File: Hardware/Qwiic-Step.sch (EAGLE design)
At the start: 53 parts, among them J1 PTH, J2 Qwiic Right Angle, J3 POWER_JACKSUPER_BOMB_DIGITY, J4 Qwiic Right Angle, J5 ISP, U1 A49885MM, U2 ATMEGA328P_TQFP, Y1 16MHz

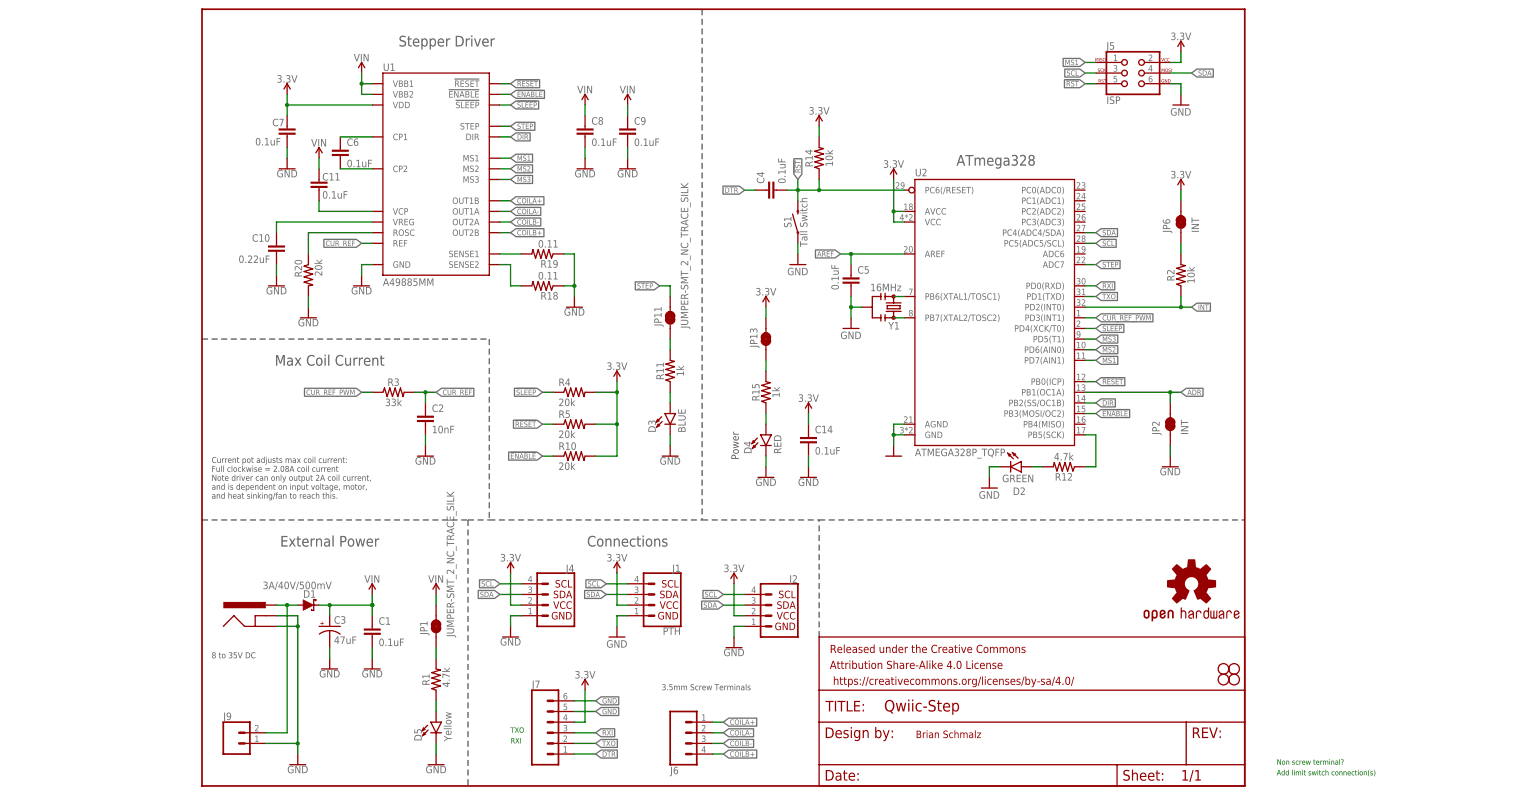
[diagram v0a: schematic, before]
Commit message: New board layout. Added current sense.
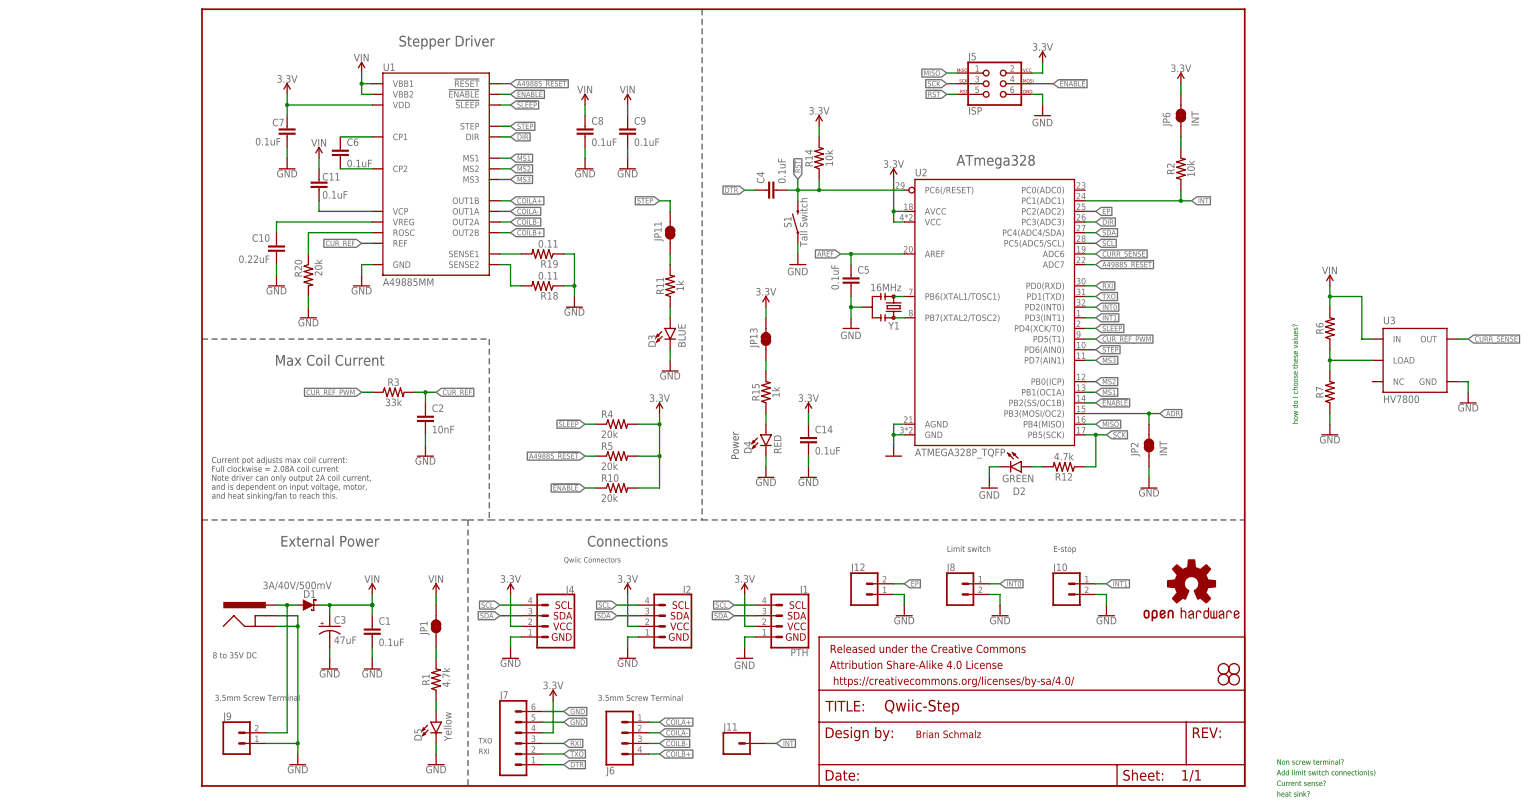
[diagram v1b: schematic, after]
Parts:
- added J10, J8: (no value), SparkFun-Connectors:CONN_02-JST-2MM-SMT
- added J11: (no value), SparkFun-Connectors:CONN_01PTH_NO_SILK_YES_STOP
- added J12: (no value), SparkFun-Connectors:CONN_021X02_NO_SILK
- added R6, R7: (no value), SparkFun-Resistors:RESISTOR0603
- added U3: HV7800, SparkFun-IC-Special-Function:HV7800
- J5: device SparkFun-Connectors:AVR_SPI_PROG_3X2PTH -> SparkFun-Connectors:AVR_SPI_PROG_3X2TESTPOINTS
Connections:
- removed net !RESET!: R5.1, U1.!RESET!, U2.PB0(ICP)
- new net A49885_!RESET!: R5.1, U1.!RESET!, U2.ADC7
- new net CURR_SENSE: U2.ADC6, U3.OUT
- new net EP: J12.2, U2.PC2(ADC2)
- new net INT0: J8.2, U2.PD2(INT0)
- new net INT1: J10.2, U2.PD3(INT1)
- new net MISO: J5.1, U2.PB4(MISO)
- new net N$6: R6.1, R7.2, U3.LOAD
- net !ENABLE!: now also J5.4, U2.PB2(SS/OC1B); no longer U2.PB3(MOSI/OC2)
- net ADR: now also U2.PB3(MOSI/OC2); no longer U2.PB1(OC1A)
- net CUR_REF_PWM: now also U2.PD5(T1); no longer U2.PD3(INT1)
- net DIR: now also U2.PC3(ADC3); no longer U2.PB2(SS/OC1B)
- net GND: now also J10.1, J12.1, J8.1, R7.1, U3.GND
- net INT: now also J11.1, U2.PC1(ADC1); no longer U2.PD2(INT0)
- net MS1: now also U2.PB1(OC1A); no longer J5.1, U2.PD7(AIN1)
- net MS2: now also U2.PB0(ICP); no longer U2.PD6(AIN0)
- net MS3: now also U2.PD7(AIN1); no longer U2.PD5(T1)
- net SCK: now also J5.3
- net SCL: no longer J5.3
- net SDA: no longer J5.4
- net STEP: now also U2.PD6(AIN0); no longer U2.ADC7
- net VIN: now also R6.2, U3.IN
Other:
- note added: "3.5mm Screw Terminal"
- note added: "Current sense?"
- note added: "E-stop"
- note added: "Limit switch"
- note added: "Qwiic Connectors"
- note added: "heat sink?"
- note added: "how do I choose these values?"
- note removed: "3.5mm Screw Terminals"
- moved on the sheet: D3, J1, J2, J4, J5, J6, J7, JP11, JP2, JP6, R10, R11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

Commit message: Removed generated libraries and finishing up layout
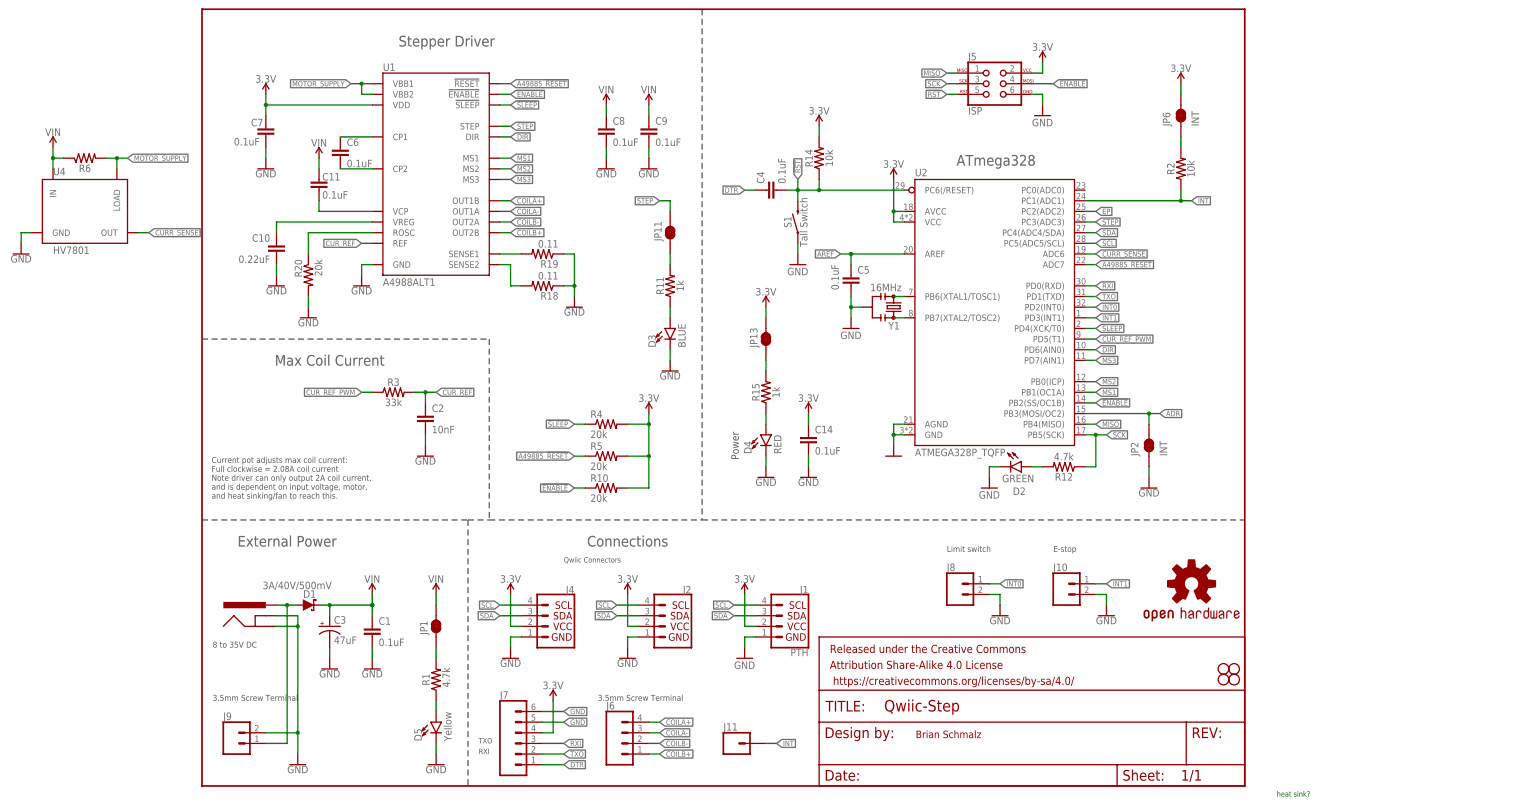
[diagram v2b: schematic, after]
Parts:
- removed J12: (no value), SparkFun-Connectors:CONN_021X02_NO_SILK
- removed R7: (no value), SparkFun-Resistors:RESISTOR0603
- removed U3: HV7800, SparkFun-IC-Special-Function:HV7800
- added U4: HV7801, SparkFun-IC-Special-Function:HV7801
- J3: value POWER_JACKSUPER_BOMB_DIGITY -> 5.5x2.1mm Barrel; device Testing:POWER_JACKSUPER_BOMB_DIGITY -> SparkFun-Connectors:POWER_JACKSMD
- J6: device SparkFun-Connectors:CONN_04SCREW -> SparkFun-Connectors:CONN_04LATCH
- J9: device SparkFun-Connectors:CONN_023.5MM -> SparkFun-Connectors:CONN_02LATCH_2
- JP10, JP7, JP8, JP9: device SparkFun-7-28-09:STAND-OFF -> SparkFun-Hardware:STAND-OFF
- U1: value A49885MM -> A4988ALT1; device SparkFun-PowerIC:A49885MM -> SparkFun-IC-Special-Function:A4988ALT1
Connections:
- removed net N$6: R6.1, R7.2, U3.LOAD
- new net MOTOR_SUPPLY: R6.2, U1.VBB1, U1.VBB2, U4.LOAD
- net COILA+: now also J6.4; no longer J6.1
- net COILA-: now also J6.3; no longer J6.2
- net COILB+: now also J6.1; no longer J6.4
- net COILB-: now also J6.2; no longer J6.3
- net CURR_SENSE: now also U4.OUT; no longer U3.OUT
- net DIR: now also U2.PD6(AIN0); no longer U2.PC3(ADC3)
- net EP: no longer J12.2
- net GND: now also J9.2, U4.GND; no longer J12.1, J9.1, R7.1, U3.GND
- net N$7: now also J9.1; no longer J9.2
- net STEP: now also U2.PC3(ADC3); no longer U2.PD6(AIN0)
- net VIN: now also R6.1, U4.IN; no longer R6.2, U1.VBB1, U1.VBB2, U3.IN
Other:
- note removed: "Add limit switch connection(s)"
- note removed: "Current sense?"
- note removed: "Non screw terminal?"
- note removed: "how do I choose these values?"
- moved on the sheet: C7, C8, C9, J6, R10, R4, R5, R6

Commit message: Final board layout
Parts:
- R6: value (none) -> 0.25OHM_RES; device SparkFun-Resistors:RESISTOR0603 -> qwiic_step:0.25OHM_RES

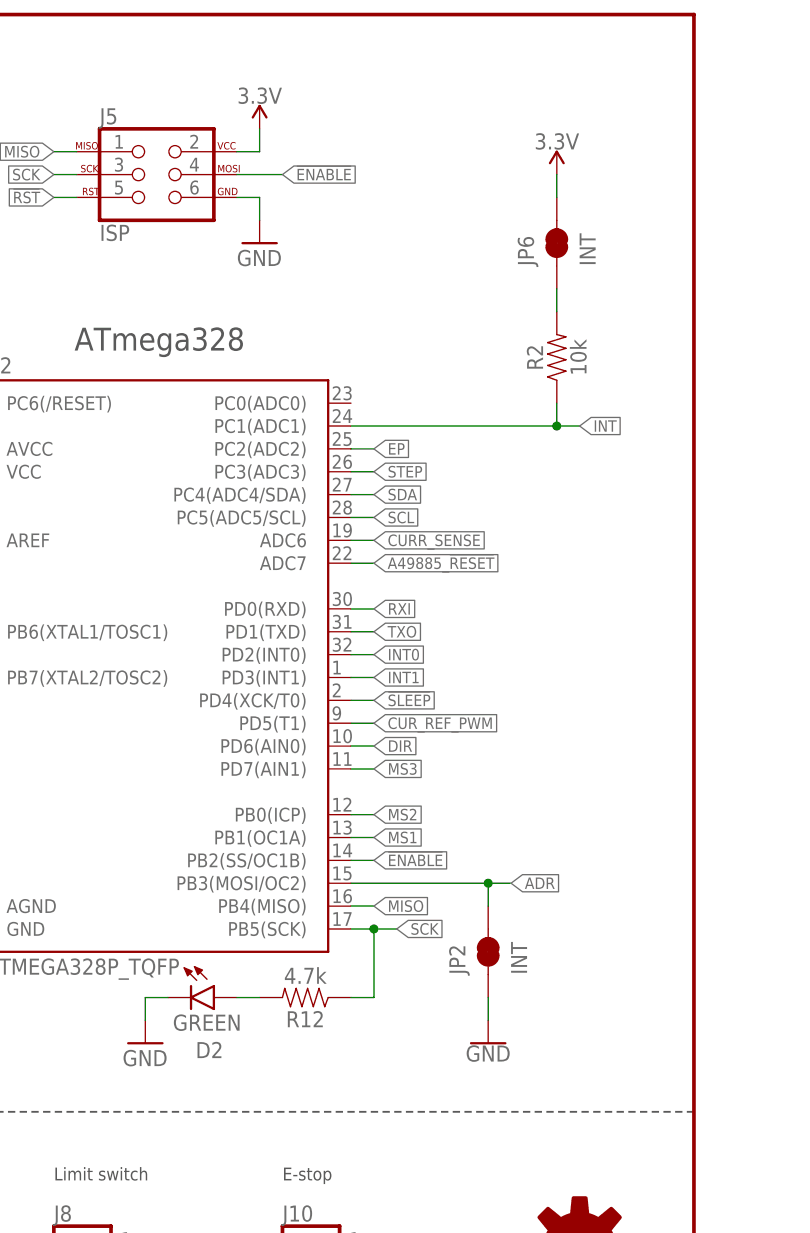
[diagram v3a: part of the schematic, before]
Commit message: Superficial function name changes and board update
Rev 2 of Qwiic Step board! Fixed: MOSI was not connected to ISP pins! Adjusted MOSI and ADR jumper
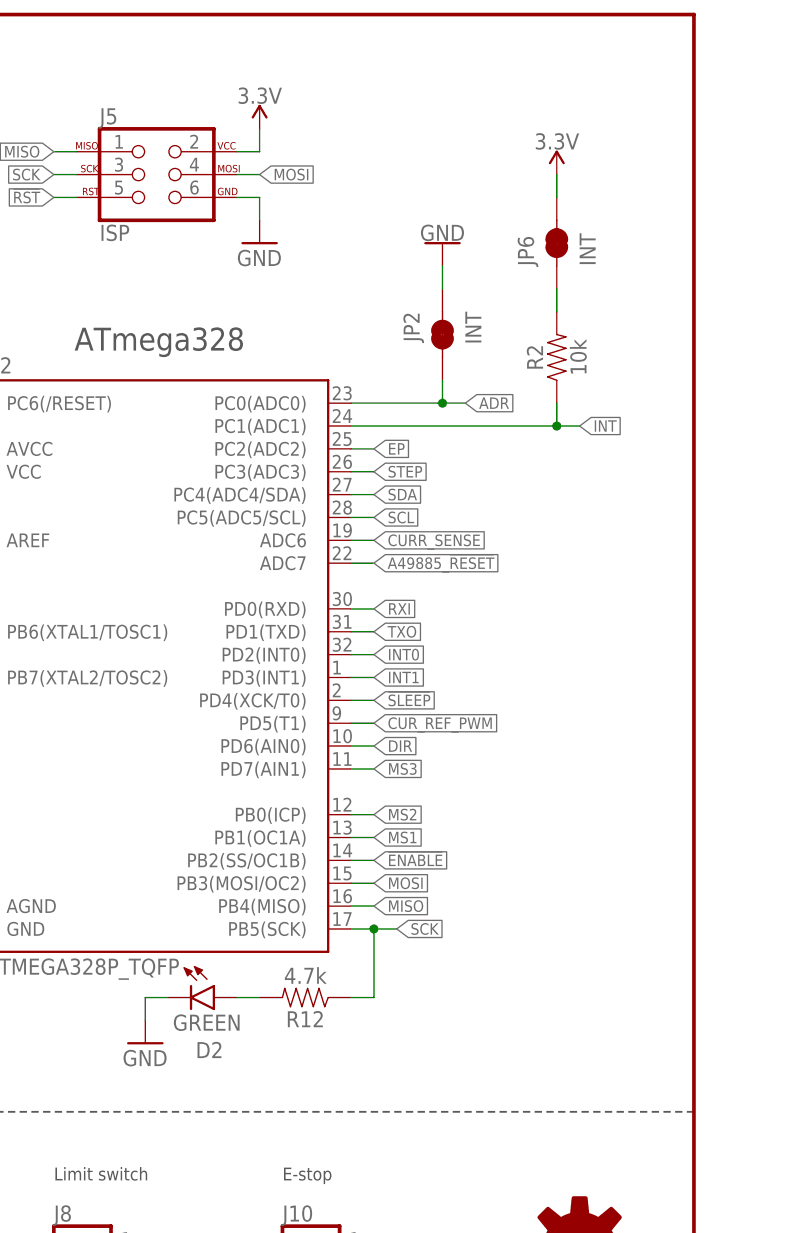
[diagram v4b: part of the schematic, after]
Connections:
- new net MOSI: J5.4, U2.PB3(MOSI/OC2)
- net !ENABLE!: no longer J5.4
- net ADR: now also U2.PC0(ADC0); no longer U2.PB3(MOSI/OC2)
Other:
- moved on the sheet: JP2
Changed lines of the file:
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@@
 <attribute name="VALUE" x="147.32" y="160.274" size="1.778" layer="96" align="bottom-center"/>
 </instance>
-<instance part="GND20" gate="1" x="226.06" y="71.12" smashed="yes" rot="MR0">
-<attribute name="VALUE" x="226.06" y="70.866" size="1.778" layer="96" rot="MR0" align="top-center"/>
+<instance part="GND20" gate="1" x="220.98" y="160.02" smashed="yes" rot="R180">
+<attribute name="VALUE" x="220.98" y="160.274" size="1.778" layer="96" rot="R180" align="top-center"/>
 </instance>
 <instance part="SUPPLY23" gate="G$1" x="144.78" y="88.9" smashed="yes">
@@
 <attribute name="VALUE" x="54.864" y="84.201" size="1.778" layer="96" font="vector"/>
 </instance>
-<instance part="JP2" gate="G$1" x="226.06" y="81.28" smashed="yes" rot="R90">
-<attribute name="NAME" x="223.52" y="78.74" size="1.778" layer="95" font="vector" rot="R90"/>
-<attribute name="VALUE" x="228.6" y="78.74" size="1.778" layer="96" font="vector" rot="R90" align="top-left"/>
+<instance part="JP2" gate="G$1" x="220.98" y="149.86" smashed="yes" rot="MR270">
+<attribute name="NAME" x="218.44" y="152.4" size="1.778" layer="95" font="vector" rot="MR270"/>
+<attribute name="VALUE" x="223.52" y="152.4" size="1.778" layer="96" font="vector" rot="MR270" align="top-left"/>
 </instance>
 <instance part="D5" gate="G$1" x="55.88" y="15.24" smashed="yes">
@@
 <segment>
 <pinref part="GND20" gate="1" pin="GND"/>
-<wire x1="226.06" y1="73.66" x2="226.06" y2="76.2" width="0.1524" layer="91"/>
+<wire x1="220.98" y1="157.48" x2="220.98" y2="154.94" width="0.1524" layer="91"/>
 <pinref part="JP2" gate="G$1" pin="1"/>
 </segment>
@@
 <label x="73.66" y="165.1" size="1.27" layer="95" rot="MR180" xref="yes"/>
 <pinref part="U1" gate="G$1" pin="!ENABLE!"/>
-</segment>
-<segment>
-<wire x1="198.12" y1="167.64" x2="203.2" y2="167.64" width="0.1524" layer="91"/>
-<pinref part="J5" gate="G$1" pin="4"/>
-<label x="203.2" y="167.64" size="1.27" layer="95" font="vector" xref="yes"/>
 </segment>
 <segment>
@@
 <net name="ADR" class="0">
 <segment>
-<pinref part="U2" gate="U1" pin="PB3(MOSI/OC2)"/>
-<wire x1="226.06" y1="88.9" x2="228.6" y2="88.9" width="0.1524" layer="91"/>
-<wire x1="226.06" y1="86.36" x2="226.06" y2="88.9" width="0.1524" layer="91"/>
-<label x="228.6" y="88.9" size="1.27" layer="95" xref="yes"/>
+<wire x1="220.98" y1="142.24" x2="223.52" y2="142.24" width="0.1524" layer="91"/>
+<wire x1="220.98" y1="144.78" x2="220.98" y2="142.24" width="0.1524" layer="91"/>
+<label x="223.52" y="142.24" size="1.27" layer="95" rot="MR180" xref="yes"/>
 <pinref part="JP2" gate="G$1" pin="2"/>
-<wire x1="210.82" y1="88.9" x2="226.06" y2="88.9" width="0.1524" layer="91"/>
-<junction x="226.06" y="88.9"/>
+<pinref part="U2" gate="U1" pin="PC0(ADC0)"/>
+<wire x1="210.82" y1="142.24" x2="220.98" y2="142.24" width="0.1524" layer="91"/>
+<junction x="220.98" y="142.24"/>
 </segment>
 </net>
@@
 </segment>
 </net>
+<net name="MOSI" class="0">
+<segment>
+<pinref part="J5" gate="G$1" pin="4"/>
+<wire x1="198.12" y1="167.64" x2="200.66" y2="167.64" width="0.1524" layer="91"/>
+<label x="200.66" y="167.64" size="1.27" layer="95" xref="yes"/>
+</segment>
+<segment>
+<pinref part="U2" gate="U1" pin="PB3(MOSI/OC2)"/>
+<wire x1="210.82" y1="88.9" x2="213.36" y2="88.9" width="0.1524" layer="91"/>
+<label x="213.36" y="88.9" size="1.27" layer="95" xref="yes"/>
+</segment>
+</net>
